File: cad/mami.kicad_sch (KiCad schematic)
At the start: 86 parts, among them SW1 SW_Push, SW10 SW_Push, SW11 SW_Push, SW12 SW_Push, SW13 SW_Push, SW14 SW_Push, SW15 SW_Push, SW16 SW_Push, SW17 SW_Push, SW18 SW_Push, SW19 SW_Push, SW2 SW_Push, SW20 SW_Push, SW21 SW_Push, SW22 SW_Push, SW23 SW_Push, SW24 SW_Push, SW25 SW_Push, SW26 SW_Push, SW27 SW_Push, SW28 SW_Push, SW29 SW_Push, SW3 SW_Push, SW30 SW_Push, SW31 SW_Push, SW32 SW_Push, SW33 SW_Push, SW34 SW_Push, SW35 SW_Push, SW36 SW_Push, SW37 SW_Push, SW38 SW_Push, SW39 SW_Push, SW4 SW_Push, SW40 SW_Push, SW41 SW_Push, SW42 SW_Push, SW43 ResetSW, SW5 SW_Push, SW6 SW_Push, SW7 SW_Push, SW8 SW_Push, SW9 SW_Push, U1 ProMicro

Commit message: symmetric schema update pcb
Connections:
- net col2: now also U1.20 (F4/A3); no longer U1.9 (6/D7)
- net col3: now also U1.19 (F5/A2); no longer U1.10 (7/E6)
- net col4: now also U1.18 (F6/A1); no longer U1.11 (8/B4)
- net col5: now also U1.17 (F7/A0); no longer U1.12 (9/B5)
- net row0: now also U1.16 (B1/15); no longer U1.20 (F4/A3)
- net row1: now also U1.15 (B3/14); no longer U1.19 (F5/A2)
- net row2: now also U1.14 (B2/16)
- net row3: now also U1.13 (B6/10); no longer U1.18 (F6/A1)
- net row4: now also U1.9 (6/D7); no longer U1.17 (F7/A0)
- net row5: now also U1.10 (7/E6); no longer U1.16 (B1/15)
- net row6: now also U1.11 (8/B4); no longer U1.15 (B3/14)
- net row7: now also U1.12 (9/B5); no longer U1.14 (B2/16)
- no-connect marks 6 -> 5
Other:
- moved on the sheet: D1, D10, D11, D12, D13, D14, D15, D16, D17, D18, D19, D2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

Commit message: 回路図エディターをbattery有り＋LED有りに変更
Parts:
- removed U1: ProMicro, kbd:ProMicro, symbol kbd:ProMicro
- added J2: Conn_01x02, kbd_Parts:Battery_BMP_2pin, symbol Connector_Generic:Conn_01x02
- added L1, L10, L11, L12, L13, L14, L15, L16, L17, L18, L19, L2, L20, L21, L22, L23, L24, L25, L26, L27, L28, L29, L3, L30, L31, L32, L33, L34, L35, L36, L37, L38, L39, L4, L40, L41, L42, L5, L6, L7, L8, L9: SK6812MINI, kbd_Parts:LED_SK6812MINI-E_BL, symbol Salicylic_kbd:LED_SK6812MINI-E
- added SW45: SW_SPDT, symbol Switch:SW_SPDT
- added U1: nice_nano, symbol mylib:nice_nano
- renumbered D7 to D10, D39 to D36, D36 to D37, D37 to D38, D38 to D39, D8 to D7, D9 to D8, D10 to D9, SW7 to SW10, SW39 to SW36, SW36 to SW37, SW37 to SW38, SW38 to SW39, SW8 to SW7, SW9 to SW8, SW10 to SW9
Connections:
- net GND: now also J2.2 (Pin_2), L1.2 (VSS), L10.2 (VSS), L11.2 (VSS), L12.2 (VSS), L13.2 (VSS), L14.2 (VSS), L15.2 (VSS), L16.2 (VSS), L17.2 (VSS), L18.2 (VSS), L19.2 (VSS), L2.2 (VSS), L20.2 (VSS), L21.2 (VSS), L22.2 (VSS), L23.2 (VSS), L24.2 (VSS), L25.2 (VSS), L26.2 (VSS), L27.2 (VSS), L28.2 (VSS), L29.2 (VSS), L3.2 (VSS), L30.2 (VSS), L31.2 (VSS), L32.2 (VSS), L33.2 (VSS), L34.2 (VSS), L35.2 (VSS), L36.2 (VSS), L37.2 (VSS), L38.2 (VSS), L39.2 (VSS), L4.2 (VSS), L40.2 (VSS), L41.2 (VSS), L42.2 (VSS), L5.2 (VSS), L6.2 (VSS), L7.2 (VSS), L8.2 (VSS), L9.2 (VSS), U1.23 (GND), U1.3 (GND), U1.30 (GND), U1.4 (GND)
- net VCC: now also L1.4 (VDD), L10.4 (VDD), L11.4 (VDD), L12.4 (VDD), L13.4 (VDD), L14.4 (VDD), L15.4 (VDD), L16.4 (VDD), L17.4 (VDD), L18.4 (VDD), L19.4 (VDD), L2.4 (VDD), L20.4 (VDD), L21.4 (VDD), L22.4 (VDD), L23.4 (VDD), L24.4 (VDD), L25.4 (VDD), L26.4 (VDD), L27.4 (VDD), L28.4 (VDD), L29.4 (VDD), L3.4 (VDD), L30.4 (VDD), L31.4 (VDD), L32.4 (VDD), L33.4 (VDD), L34.4 (VDD), L35.4 (VDD), L36.4 (VDD), L37.4 (VDD), L38.4 (VDD), L39.4 (VDD), L4.4 (VDD), L40.4 (VDD), L41.4 (VDD), L42.4 (VDD), L5.4 (VDD), L6.4 (VDD), L7.4 (VDD), L8.4 (VDD), L9.4 (VDD), U1.21 (VCC)
- net col0: now also U1.20 (AIN7/P0.31)
- net col1: now also U1.19 (AIN5/P0.29); no longer SW10.1, SW36.1
- net col2: now also SW10.1, SW36.1, U1.18 (AIN0/P0.02)
- net col3: now also U1.5 (P0.17)
- net col4: now also U1.6 (P0.20)
- net col5: now also U1.7 (P0.22)
- net reset: now also U1.22 (RST)
- net row0: now also U1.16 (P1.13)
- net row1: now also U1.15 (P1.11)
- net row2: now also U1.14 (NFC2/P0.10)
- net row3: now also U1.13 (NFC1/P0.09)
- net row4: now also U1.9 (P1.00)
- net row5: now also U1.10 (P0.11)
- net row6: now also U1.11 (P1.04)
- net row7: now also U1.12 (P1.06)
- new net: L19.1 (DOUT), L20.3 (DIN)
- new net: L18.1 (DOUT), L19.3 (DIN)
- new net: L39.1 (DOUT), L40.3 (DIN)
- new net: L38.1 (DOUT), L39.3 (DIN)
- new net: L7.1 (DOUT), L8.3 (DIN)
- new net: L6.1 (DOUT), L7.3 (DIN)
- new net: L4.1 (DOUT), L5.3 (DIN)
- new net: L3.1 (DOUT), L4.3 (DIN)
- new net: L26.1 (DOUT), L27.3 (DIN)
- new net: L25.1 (DOUT), L26.3 (DIN)
- new net: L17.1 (DOUT), L18.3 (DIN)
- new net: L41.1 (DOUT), L42.3 (DIN)
- new net: L29.1 (DOUT), L30.3 (DIN)
- new net: L28.1 (DOUT), L29.3 (DIN)
- new net: L5.1 (DOUT), L6.3 (DIN)
- new net: L1.1 (DOUT), L2.3 (DIN)
- new net: L27.1 (DOUT), L28.3 (DIN)
- new net: L10.1 (DOUT), L11.3 (DIN)
- new net: L10.3 (DIN), L9.1 (DOUT)
- new net: L11.1 (DOUT), L12.3 (DIN)
- new net: L16.1 (DOUT), L17.3 (DIN)
- new net: L8.1 (DOUT), L9.3 (DIN)
- new net: L24.1 (DOUT), L25.3 (DIN)
- new net: L12.1 (DOUT), L13.3 (DIN)
- new net: L40.1 (DOUT), L41.3 (DIN)
- new net: L2.1 (DOUT), L3.3 (DIN)
- new net: L37.1 (DOUT), L38.3 (DIN)
- new net: L36.1 (DOUT), L37.3 (DIN)
- new net: L35.1 (DOUT), L36.3 (DIN)
- new net: L21.1 (DOUT), L22.3 (DIN)
- new net: L20.1 (DOUT), L21.3 (DIN)
- new net: L31.1 (DOUT), L32.3 (DIN)
- new net: L30.1 (DOUT), L31.3 (DIN)
- new net: L15.1 (DOUT), L16.3 (DIN)
- new net: L34.1 (DOUT), L35.3 (DIN)
- new net: L33.1 (DOUT), L34.3 (DIN)
- new net: L22.1 (DOUT), L23.3 (DIN)
- new net: L23.1 (DOUT), L24.3 (DIN)
- new net: L14.1 (DOUT), L15.3 (DIN)
- new net: L13.1 (DOUT), L14.3 (DIN)
- new net: L32.1 (DOUT), L33.3 (DIN)
- new net B+: SW45.1 (A), U1.34 (BATIN/P0.04)
- new net BAT+: J2.1 (Pin_1), SW45.2 (B)
- new net LED: L1.3 (DIN), U1.1 (TX0/P0.06)
- no-connect marks 5 -> 9
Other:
- moved on the sheet: D10, D36, SW10, SW36, SW43

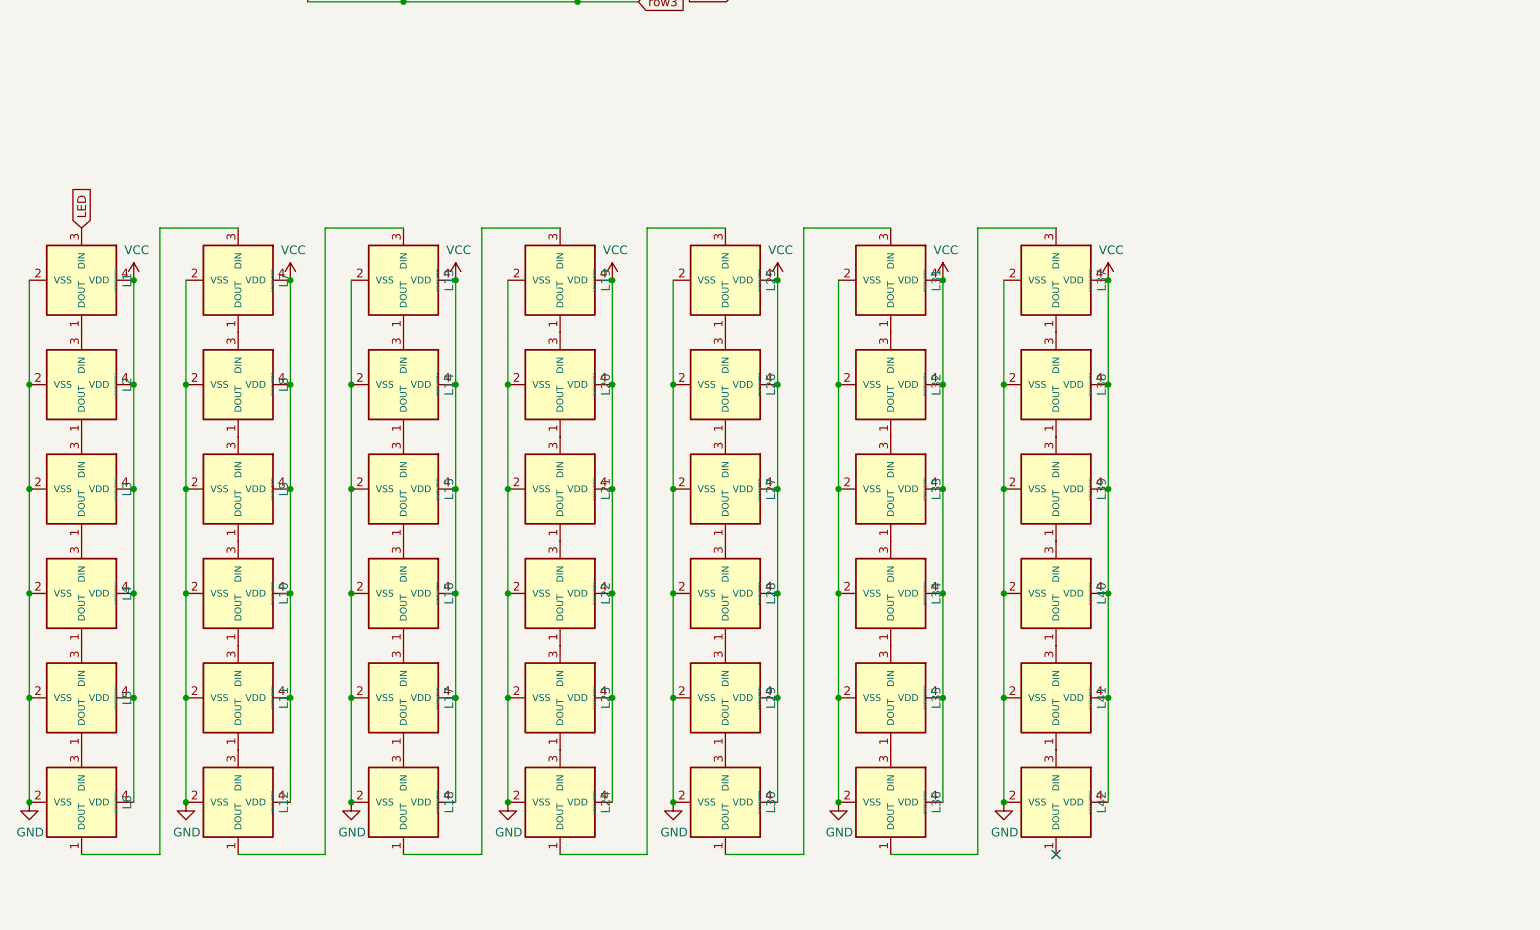
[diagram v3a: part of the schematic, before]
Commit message: LEDのフットプリント更新
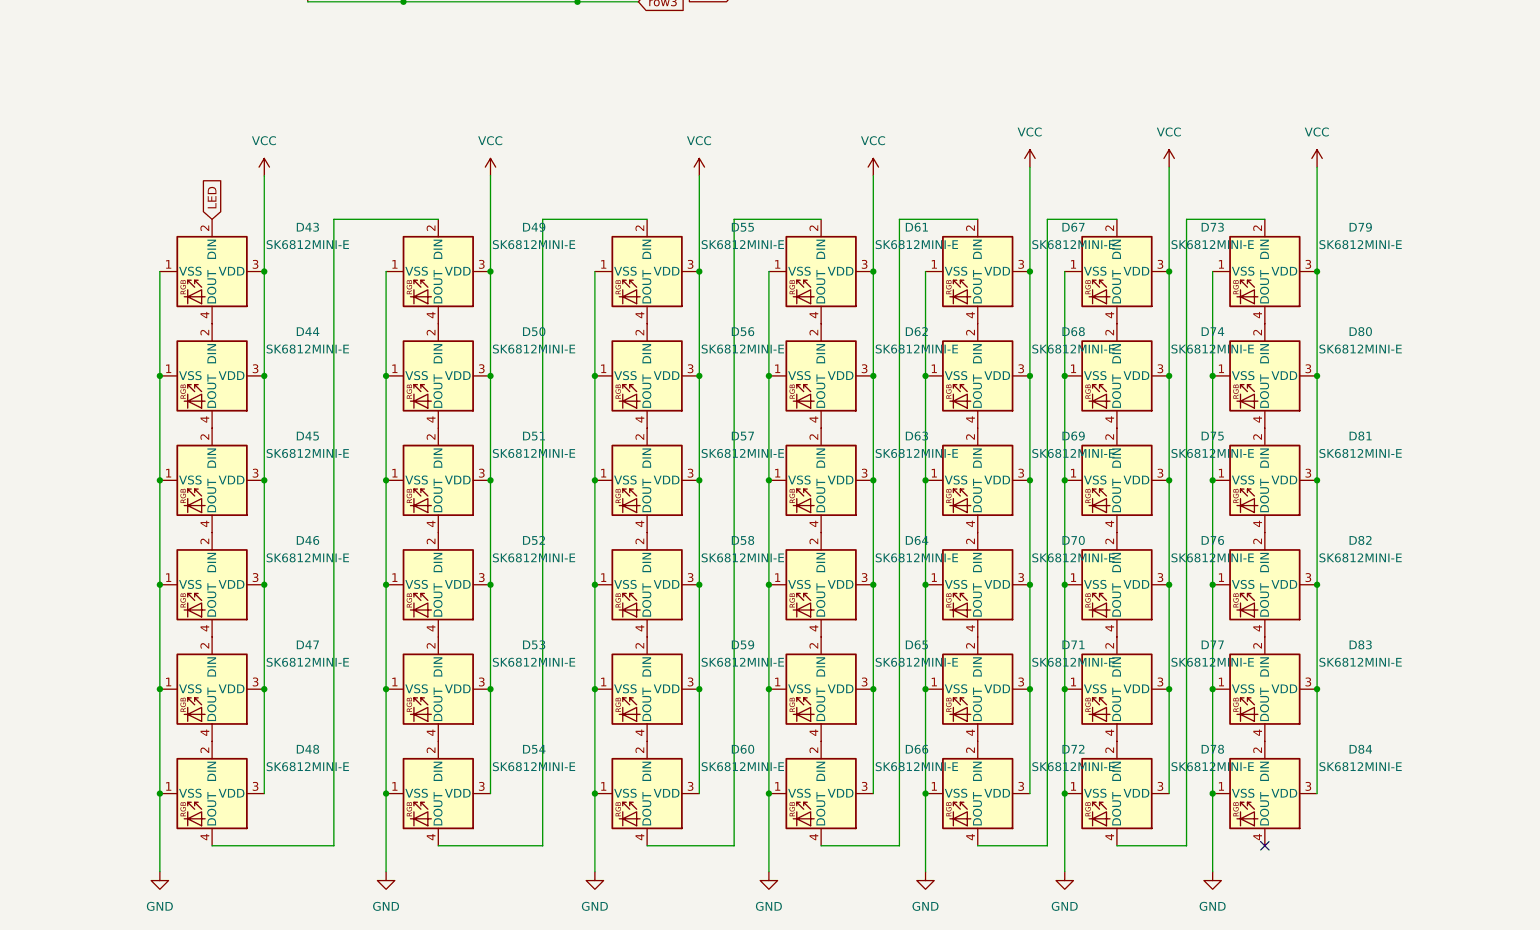
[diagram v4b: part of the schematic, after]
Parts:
- removed L1, L10, L11, L12, L13, L14, L15, L16, L17, L18, L19, L2, L20, L21, L22, L23, L24, L25, L26, L27, L28, L29, L3, L30, L31, L32, L33, L34, L35, L36, L37, L38, L39, L4, L40, L41, L42, L5, L6, L7, L8, L9: SK6812MINI, kbd_Parts:LED_SK6812MINI-E_BL, symbol Salicylic_kbd:LED_SK6812MINI-E
- added D43, D44, D45, D46, D47, D48, D49, D50, D51, D52, D53, D54, D55, D56, D57, D58, D59, D60, D61, D62, D63, D64, D65, D66, D67, D68, D69, D70, D71, D72, D73, D74, D75, D76, D77, D78, D79, D80, D81, D82, D83, D84: SK6812MINI-E, LED_SMD:LED_SK6812MINI-E_3.2x2.8mm_P1.5mm_ReverseMount, symbol LED:SK6812MINI-E
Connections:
- net GND: now also D43.1 (VSS), D44.1 (VSS), D45.1 (VSS), D46.1 (VSS), D47.1 (VSS), D48.1 (VSS), D49.1 (VSS), D50.1 (VSS), D51.1 (VSS), D52.1 (VSS), D53.1 (VSS), D54.1 (VSS), D55.1 (VSS), D56.1 (VSS), D57.1 (VSS), D58.1 (VSS), D59.1 (VSS), D60.1 (VSS), D61.1 (VSS), D62.1 (VSS), D63.1 (VSS), D64.1 (VSS), D65.1 (VSS), D66.1 (VSS), D67.1 (VSS), D68.1 (VSS), D69.1 (VSS), D70.1 (VSS), D71.1 (VSS), D72.1 (VSS), D73.1 (VSS), D74.1 (VSS), D75.1 (VSS), D76.1 (VSS), D77.1 (VSS), D78.1 (VSS), D79.1 (VSS), D80.1 (VSS), D81.1 (VSS), D82.1 (VSS), D83.1 (VSS), D84.1 (VSS)
- net LED: now also D43.2 (DIN)
- net VCC: now also D43.3 (VDD), D44.3 (VDD), D45.3 (VDD), D46.3 (VDD), D47.3 (VDD), D48.3 (VDD), D49.3 (VDD), D50.3 (VDD), D51.3 (VDD), D52.3 (VDD), D53.3 (VDD), D54.3 (VDD), D55.3 (VDD), D56.3 (VDD), D57.3 (VDD), D58.3 (VDD), D59.3 (VDD), D60.3 (VDD), D61.3 (VDD), D62.3 (VDD), D63.3 (VDD), D64.3 (VDD), D65.3 (VDD), D66.3 (VDD), D67.3 (VDD), D68.3 (VDD), D69.3 (VDD), D70.3 (VDD), D71.3 (VDD), D72.3 (VDD), D73.3 (VDD), D74.3 (VDD), D75.3 (VDD), D76.3 (VDD), D77.3 (VDD), D78.3 (VDD), D79.3 (VDD), D80.3 (VDD), D81.3 (VDD), D82.3 (VDD), D83.3 (VDD), D84.3 (VDD)
- new net: D43.4 (DOUT), D44.2 (DIN)
- new net: D60.4 (DOUT), D61.2 (DIN)
- new net: D61.4 (DOUT), D62.2 (DIN)
- new net: D64.4 (DOUT), D65.2 (DIN)
- new net: D65.4 (DOUT), D66.2 (DIN)
- new net: D74.4 (DOUT), D75.2 (DIN)
- new net: D75.4 (DOUT), D76.2 (DIN)
- new net: D52.4 (DOUT), D53.2 (DIN)
- new net: D53.4 (DOUT), D54.2 (DIN)
- new net: D73.4 (DOUT), D74.2 (DIN)
- new net: D47.4 (DOUT), D48.2 (DIN)
- new net: D48.4 (DOUT), D49.2 (DIN)
- new net: D54.4 (DOUT), D55.2 (DIN)
- new net: D58.4 (DOUT), D59.2 (DIN)
- new net: D59.4 (DOUT), D60.2 (DIN)
- new net: D55.4 (DOUT), D56.2 (DIN)
- new net: D63.4 (DOUT), D64.2 (DIN)
- new net: D81.4 (DOUT), D82.2 (DIN)
- new net: D82.4 (DOUT), D83.2 (DIN)
- new net: D50.4 (DOUT), D51.2 (DIN)
- new net: D51.4 (DOUT), D52.2 (DIN)
- new net: D71.4 (DOUT), D72.2 (DIN)
- new net: D72.4 (DOUT), D73.2 (DIN)
- new net: D49.4 (DOUT), D50.2 (DIN)
- new net: D67.4 (DOUT), D68.2 (DIN)
- new net: D68.4 (DOUT), D69.2 (DIN)
- new net: D44.4 (DOUT), D45.2 (DIN)
- new net: D83.4 (DOUT), D84.2 (DIN)
- new net: D69.4 (DOUT), D70.2 (DIN)
- new net: D77.4 (DOUT), D78.2 (DIN)
- new net: D78.4 (DOUT), D79.2 (DIN)
- new net: D45.4 (DOUT), D46.2 (DIN)
- new net: D46.4 (DOUT), D47.2 (DIN)
- new net: D76.4 (DOUT), D77.2 (DIN)
- new net: D79.4 (DOUT), D80.2 (DIN)
- new net: D70.4 (DOUT), D71.2 (DIN)
- new net: D80.4 (DOUT), D81.2 (DIN)
- new net: D56.4 (DOUT), D57.2 (DIN)
- new net: D57.4 (DOUT), D58.2 (DIN)
- new net: D62.4 (DOUT), D63.2 (DIN)
- new net: D66.4 (DOUT), D67.2 (DIN)

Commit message: LED向き変更
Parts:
- removed J2: Conn_01x02, kbd_Parts:Battery_BMP_2pin, symbol Connector_Generic:Conn_01x02
- added J1: Conn_01x02_Pin, symbol Connector:Conn_01x02_Pin
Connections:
- net BAT+: now also J1.2 (Pin_2)
- net GND: now also J1.1 (Pin_1)
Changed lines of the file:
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@@
 	(global_label "BAT+"
 		(shape input)
-		(at 295.91 101.6 0)
-		(fields_autoplaced yes)
-		(effects
-			(font
-				(size 1.27 1.27)
-			)
-			(justify left)
-		)
-		(property "Intersheetrefs" "${INTERSHEET_REFS}"
-			(at 303.7938 101.6 0)
-			(hide yes)
-			(show_name no)
-			(do_not_autoplace no)
-			(effects
-				(font
-					(size 1.27 1.27)
-				)
-				(justify left)
-			)
-		)
-	)
-	(global_label "BAT+"
-		(shape input)
 		(at 356.87 69.85 180)
 		(fields_autoplaced yes)
@@
 		)
 	)
+	(global_label "BAT+"
+		(shape input)
+		(at 275.59 113.03 0)
+		(fields_autoplaced yes)
+		(effects
+			(font
+				(size 1.27 1.27)
+			)
+			(justify left)
+		)
+		(property "Intersheetrefs" "${INTERSHEET_REFS}"
+			(at 283.4738 113.03 0)
+			(hide yes)
+			(show_name no)
+			(do_not_autoplace no)
+			(effects
+				(font
+					(size 1.27 1.27)
+				)
+				(justify left)
+			)
+		)
+	)
 	(global_label "col4"
 		(shape input)
@@
 	)
 	(symbol
-		(lib_id "Connector_Generic:Conn_01x02")
-		(at 290.83 101.6 180)
-		(unit 1)
-		(body_style 1)
-		(exclude_from_sim no)
-		(in_bom yes)
-		(on_board yes)
-		(in_pos_files yes)
-		(dnp no)
-		(property "Reference" "J2"
-			(at 292.862 93.345 0)
-			(show_name no)
-			(do_not_autoplace no)
-			(effects
-				(font
-					(size 1.27 1.27)
-				)
-			)
-		)
-		(property "Value" "Conn_01x02"
-			(at 292.862 95.6564 0)
-			(show_name no)
-			(do_not_autoplace no)
-			(effects
-				(font
-					(size 1.27 1.27)
-				)
-			)
-		)
-		(property "Footprint" "kbd_Parts:Battery_BMP_2pin"
-			(at 290.83 101.6 0)
-			(hide yes)
-			(show_name no)
-			(do_not_autoplace no)
-			(effects
-				(font
-					(size 1.27 1.27)
-				)
-			)
-		)
-		(property "Datasheet" ""
-			(at 290.83 101.6 0)
-			(hide yes)
-			(show_name no)
-			(do_not_autoplace no)
-			(effects
-				(font
-					(size 1.27 1.27)
-				)
-			)
-		)
-		(property "Description" ""
-			(at 290.83 101.6 0)
-			(show_name no)
-			(do_not_autoplace no)
-			(effects
-				(font
-					(size 1.27 1.27)
-				)
-			)
-		)
-		(pin "1"
-		)
-		(pin "2"
-		)
-		(instances
-			(project "mami"
-				(path "/03b8bdc3-a3aa-42a3-983b-e8e3ae7b5f4d"
-					(reference "J2")
-					(unit 1)
-				)
-			)
-		)
-	)
-	(symbol
 		(lib_id "Switch:SW_Push")
 		(at 173.99 88.9 0)
@@
 	)
 	(symbol
+		(lib_id "power:GND")
+		(at 275.59 110.49 90)
+		(unit 1)
+		(body_style 1)
+		(exclude_from_sim no)
+		(in_bom yes)
+		(on_board yes)
+		(in_pos_files yes)
+		(dnp no)
+		(fields_autoplaced yes)
+		(property "Reference" "#PWR015"
+			(at 281.94 110.49 0)
+			(hide yes)
+			(show_name no)
+			(do_not_autoplace no)
+			(effects
+				(font
+					(size 1.27 1.27)
+				)
+			)
+		)
+		(property "Value" "GND"
+			(at 279.4 110.4899 90)
+			(show_name no)
+			(do_not_autoplace no)
+			(effects
+				(font
+					(size 1.27 1.27)
+				)
+				(justify right)
+			)
+		)
+		(property "Footprint" ""
+			(at 275.59 110.49 0)
+			(hide yes)
+			(show_name no)
+			(do_not_autoplace no)
+			(effects
+				(font
+					(size 1.27 1.27)
+				)
+			)
+		)
+		(property "Datasheet" ""
+			(at 275.59 110.49 0)
+			(hide yes)
+			(show_name no)
+			(do_not_autoplace no)
+			(effects
+				(font
+					(size 1.27 1.27)
+				)
+			)
+		)
+		(property "Description" "Power symbol creates a global label with name \"GND\" , ground"
+			(at 275.59 110.49 0)
+			(hide yes)
+			(show_name no)
+			(do_not_autoplace no)
+			(effects
+				(font
+					(size 1.27 1.27)
+				)
+			)
+		)
+		(pin "1"
+		)
+		(instances
+			(project "mami"
+				(path "/03b8bdc3-a3aa-42a3-983b-e8e3ae7b5f4d"
+					(reference "#PWR015")
+					(unit 1)
+				)
+			)
+		)
+	)
+	(symbol
 		(lib_id "Switch:SW_Push")
 		(at 88.9 90.17 0)
@@
 	)
 	(symbol
-		(lib_id "power:GND")
-		(at 295.91 99.06 90)
-		(unit 1)
-		(body_style 1)
-		(exclude_from_sim no)
-		(in_bom yes)
-		(on_board yes)
-		(in_pos_files yes)
-		(dnp no)
-		(fields_autoplaced yes)
-		(property "Reference" "#PWR08"
-			(at 302.26 99.06 0)
-			(hide yes)
-			(show_name no)
-			(do_not_autoplace no)
-			(effects
-				(font
-					(size 1.27 1.27)
-				)
-			)
-		)
-		(property "Value" "GND"
-			(at 299.72 99.0599 90)
-			(show_name no)
-			(do_not_autoplace no)
-			(effects
-				(font
-					(size 1.27 1.27)
-				)
-				(justify right)
-			)
-		)
-		(property "Footprint" ""
-			(at 295.91 99.06 0)
-			(hide yes)
-			(show_name no)
-			(do_not_autoplace no)
-			(effects
-				(font
-					(size 1.27 1.27)
-				)
-			)
-		)
-		(property "Datasheet" ""
-			(at 295.91 99.06 0)
-			(hide yes)
-			(show_name no)
-			(do_not_autoplace no)
-			(effects
-				(font
-					(size 1.27 1.27)
-				)
-			)
-		)
-		(property "Description" "Power symbol creates a global label with name \"GND\" , ground"
-			(at 295.91 99.06 0)
-			(hide yes)
-			(show_name no)
-			(do_not_autoplace no)
-			(effects
-				(font
-					(size 1.27 1.27)
-				)
-			)
-		)
-		(pin "1"
-		)
-		(instances
-			(project "mami"
-				(path "/03b8bdc3-a3aa-42a3-983b-e8e3ae7b5f4d"
-					(reference "#PWR08")
-					(unit 1)
-				)
-			)
-		)
-	)
-	(symbol
 		(lib_id "Diode:1N4148W")
 		(at 179.07 50.8 90)
@@
 					(unit 1)
 				)
+			)
+		)
+	)
+	(symbol
+		(lib_id "Connector:Conn_01x02_Pin")
+		(at 270.51 110.49 0)
+		(unit 1)
+		(body_style 1)
+		(exclude_from_sim no)
+		(in_bom yes)
+		(on_board yes)
+		(in_pos_files yes)
+		(dnp no)
+		(fields_autoplaced yes)
+		(property "Reference" "J1"
+			(at 271.145 105.41 0)
+			(show_name no)
+			(do_not_autoplace no)
+			(effects
+				(font
+					(size 1.27 1.27)
+				)
+			)
+		)
+		(property "Value" "Conn_01x02_Pin"
+			(at 271.145 107.95 0)
+			(show_name no)
+			(do_not_autoplace no)
+			(effects
+				(font
+					(size 1.27 1.27)
+				)
+			)
+		)
+		(property "Footprint" ""
+			(at 270.51 110.49 0)
+			(hide yes)
+			(show_name no)
+			(do_not_autoplace no)
+			(effects
+				(font
+					(size 1.27 1.27)
+				)
+			)
+		)
+		(property "Datasheet" ""
+			(at 270.51 110.49 0)
+			(hide yes)
+			(show_name no)
+			(do_not_autoplace no)
+			(effects
+				(font
+					(size 1.27 1.27)
+				)
+			)
+		)
+		(property "Description" "Generic connector, single row, 01x02, script generated"
+			(at 270.51 110.49 0)
+			(hide yes)
+			(show_name no)
+			(do_not_autoplace no)
+			(effects
+				(font
+					(size 1.27 1.27)
+				)
+			)
+		)
+		(pin "1"
+		)
+		(pin "2"
+		)
+		(instances
+			(project "mami"
+				(path "/03b8bdc3-a3aa-42a3-983b-e8e3ae7b5f4d"
+					(reference "J1")
+					(unit 1)
+				)
